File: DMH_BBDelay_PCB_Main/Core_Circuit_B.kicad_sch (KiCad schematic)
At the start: 87 parts, among them J30 Conn_01x08, J31 Conn_01x08, J32 Conn_01x08, J33 Conn_01x08, Q8 J113, SW1 SW_DPDT_3way_x2, SW2 SW_DPDT_x2, SW4 SW_SPDT, U18 CD4053B, U5 TL074, U6 TL074, U7 V3205, U8 CD4046, U9 40106

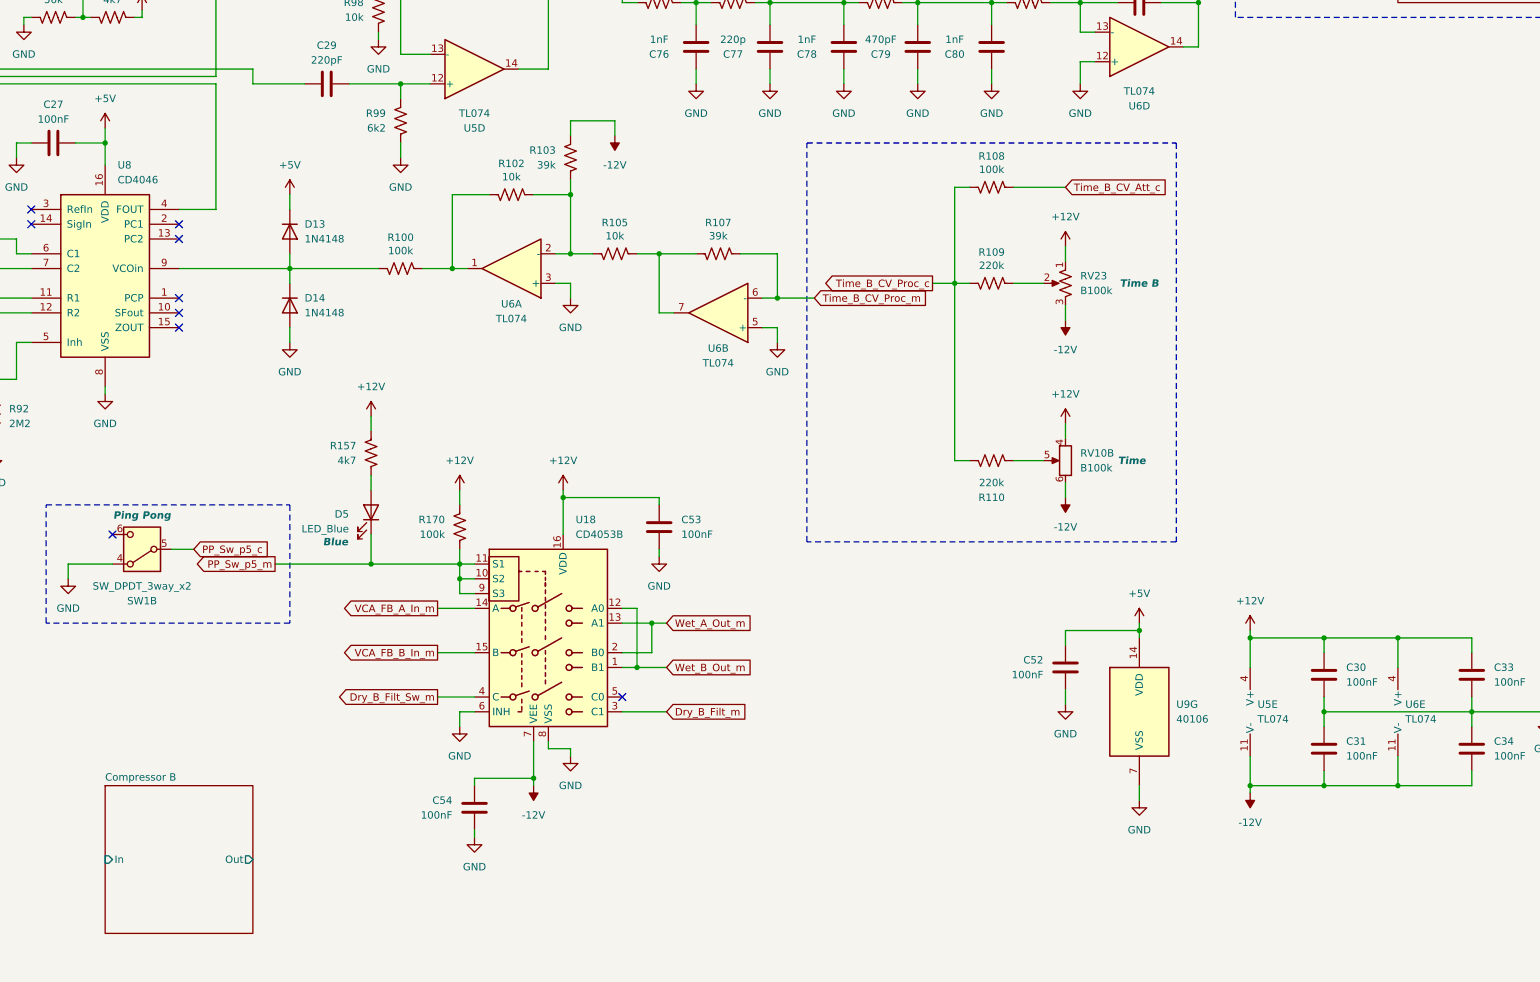
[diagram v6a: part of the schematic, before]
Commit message: Designed Expander circuits
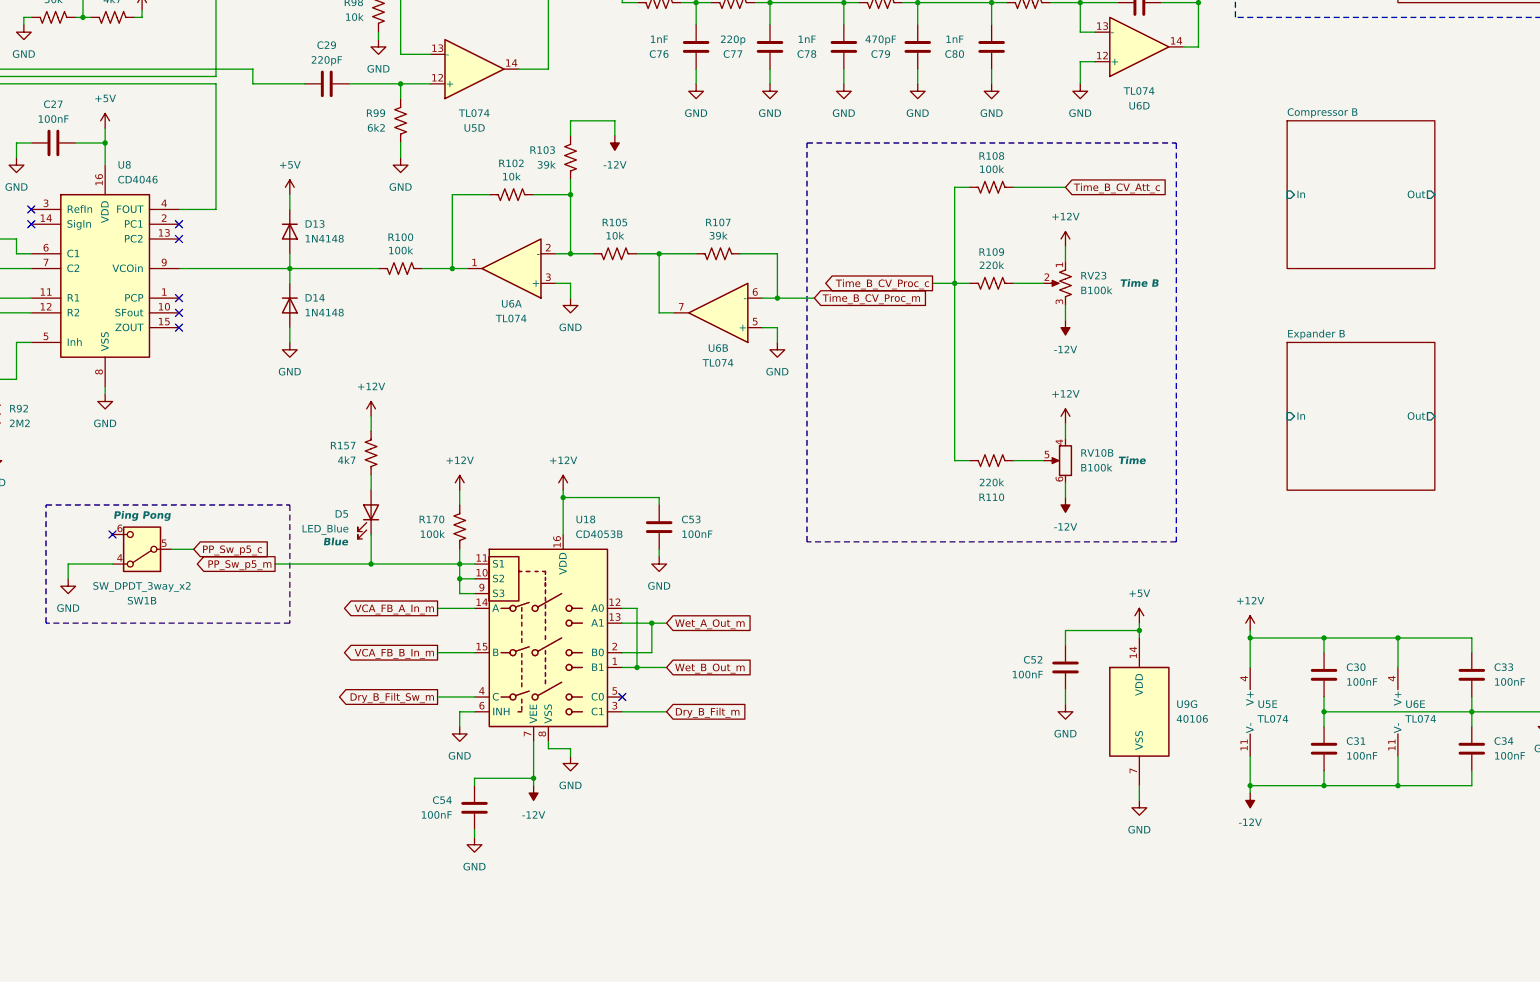
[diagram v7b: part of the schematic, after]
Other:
- added sheet Expander B (Expander_B.kicad_sch)
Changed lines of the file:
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@@
+	)
+	(sheet
+		(at 355.6 127)
+		(size 25.4 25.4)
+		(exclude_from_sim no)
+		(in_bom yes)
+		(on_board yes)
+		(dnp no)
+		(fields_autoplaced yes)
+		(stroke
+			(width 0.1524)
+			(type solid)
+		)
+		(fill
+			(color 0 0 0 0)
+		)
+		(property "Sheetname" "Compressor B"
+			(at 355.6 126.2884 0)
+			(show_name no)
+			(do_not_autoplace no)
+			(effects
+				(font
+					(size 1.27 1.27)
+				)
+				(justify left bottom)
+			)
+		)
+		(property "Sheetfile" "Compressor_B.kicad_sch"
+			(at 355.6 152.9846 0)
+			(hide yes)
+			(show_name no)
+			(do_not_autoplace no)
+			(effects
+				(font
+					(size 1.27 1.27)
+				)
+				(justify left top)
+			)
+		)
+		(pin "In" input
+			(at 355.6 139.7 180)
+			(effects
+				(font
+					(size 1.27 1.27)
+				)
+				(justify left)
+			)
+		)
+		(pin "Out" output
+			(at 381 139.7 0)
+			(effects
+				(font
+					(size 1.27 1.27)
+				)
+				(justify right)
+			)
+		)
+		(instances
+			(project "DMH_BBDelay_PCB_Main"
+				(path "/58f4306d-5387-4983-bb08-41a2313fd315/53120047-129a-4e0f-876f-6cafa2f18733"
+					(page "16")
+				)
+			)
+		)
 	)
 	(sheet
@@
 	)
 	(sheet
-		(at 152.4 241.3)
+		(at 355.6 165.1)
 		(size 25.4 25.4)
 		(exclude_from_sim no)
@@
 			(color 0 0 0 0)
 		)
-		(property "Sheetname" "Compressor B"
-			(at 152.4 240.5884 0)
+		(property "Sheetname" "Expander B"
+			(at 355.6 164.3884 0)
 			(show_name no)
 			(do_not_autoplace no)
@@
 			)
 		)
-		(property "Sheetfile" "Compressor_B.kicad_sch"
-			(at 152.4 267.2846 0)
+		(property "Sheetfile" "Expander_B.kicad_sch"
+			(at 355.6 191.0846 0)
 			(hide yes)
 			(show_name no)
@@
 		)
 		(pin "In" input
-			(at 152.4 254 180)
+			(at 355.6 177.8 180)
 			(effects
 				(font
@@
 		)
 		(pin "Out" output
-			(at 177.8 254 0)
+			(at 381 177.8 0)
 			(effects
 				(font
@@
 			(project "DMH_BBDelay_PCB_Main"
 				(path "/58f4306d-5387-4983-bb08-41a2313fd315/53120047-129a-4e0f-876f-6cafa2f18733"
-					(page "16")
+					(page "18")
 				)
 			)

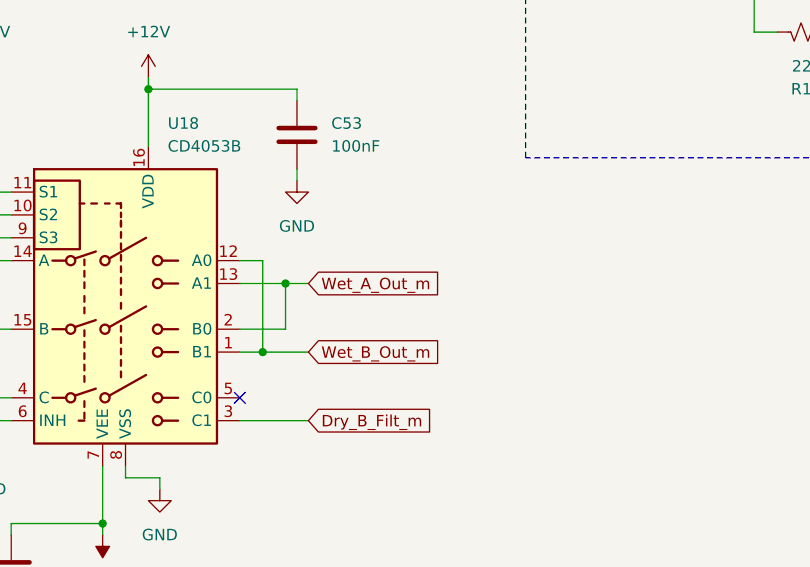
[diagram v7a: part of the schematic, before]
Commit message: Inserted compander in Channel A path
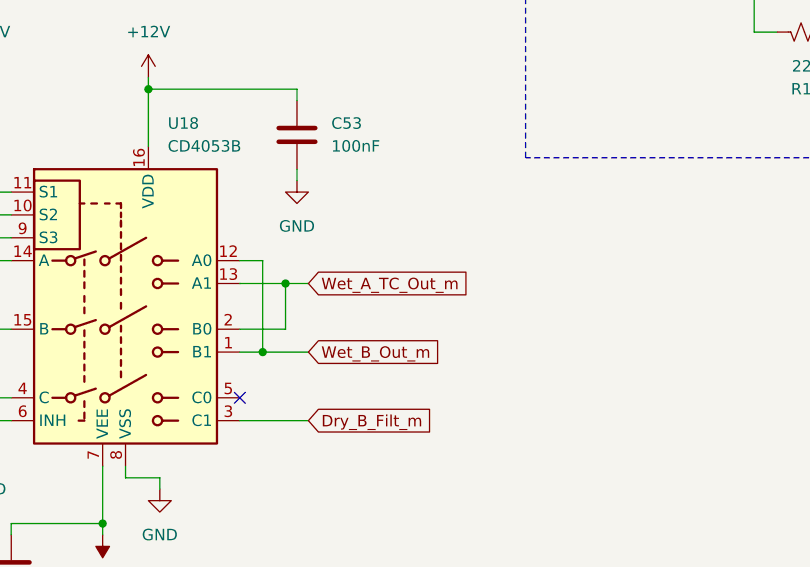
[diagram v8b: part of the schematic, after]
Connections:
- net Wet_A_Out_m renamed Wet_A_TC_Out_m
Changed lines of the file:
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@@
 		)
 	)
-	(global_label "Wet_A_Out_m"
+	(global_label "Wet_A_TC_Out_m"
 		(shape input)
 		(at 248.92 213.36 0)
@@
 		)
 		(property "Intersheetrefs" "${INTERSHEET_REFS}"
-			(at 264.0608 213.36 0)
+			(at 267.266 213.36 0)
 			(hide yes)
 			(show_name no)
